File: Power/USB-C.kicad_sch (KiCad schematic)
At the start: 27 parts, among them J1 USB_C_Receptacle_PowerOnly_6P, J2 Barrel_Jack_Switch, J3 Barrel_Jack_Switch, J4 Barrel_Jack_Switch, J5 Barrel_Jack_Switch, U1 HUSB237, U2 TPS73801

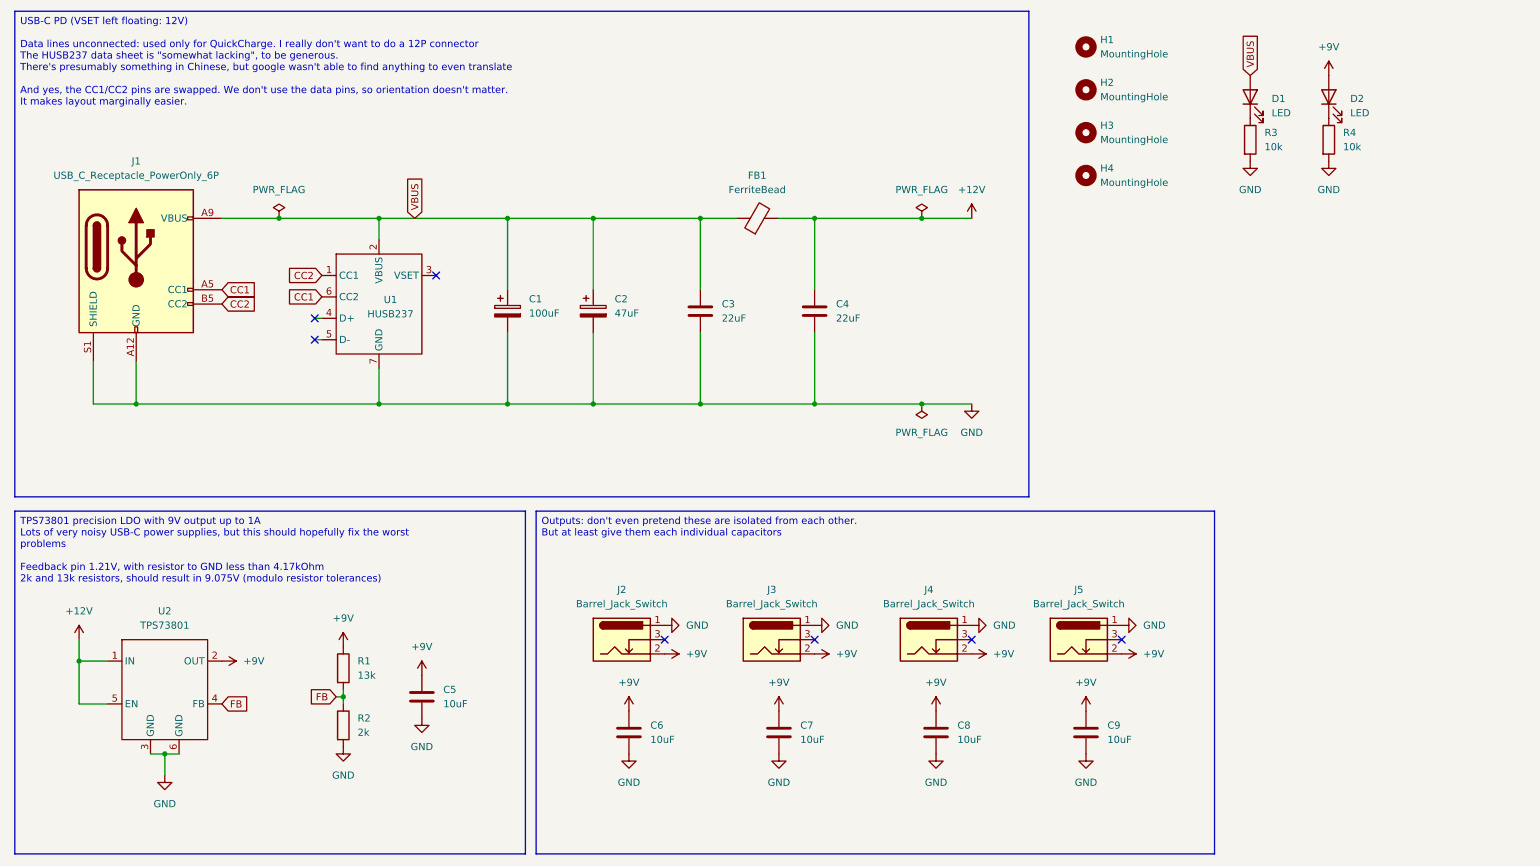
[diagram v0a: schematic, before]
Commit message: Make a switchable combo version of the USB-PD power board
So this was triggered partly by me noticing that my USB PD sources are
very inconsistent when it comes to 12V output that the original board
requested.

Several of my wall chargers do 15V but not 12V.  Of course, then some of
my battery packs are the reverse, and do 12V but not 15V output.

So there is no single thing that works for all common cases.  But 15V is
the more common option, and is required by the PD specs for anything
that claims to be 45W or more.  12V is entirely optional.

End result: add a switch to pick whether the power board requests 12V or
15V from the USB-C PD source.

And since 15V is now an option, add another LDO, and a switch to make
that LDO generate either 9V or 12V output (as per commit eb97091: "Add a
USB-C pedal power board" that already mentioned this option).

Connect the LDOs to two ports each, which also results in a certain
amount of isolation.

End result: the first two ports always output 9V, while the second two
ports can optionally provide 12V output if your USB-PD source does 15V.

The "switch" is either just a pin header with a jumper, or one of the
small slide switches that I have.  We're not doing anything fancy here.

Signed-off-by: Linus Torvalds <torvalds@linux-foundation.org>
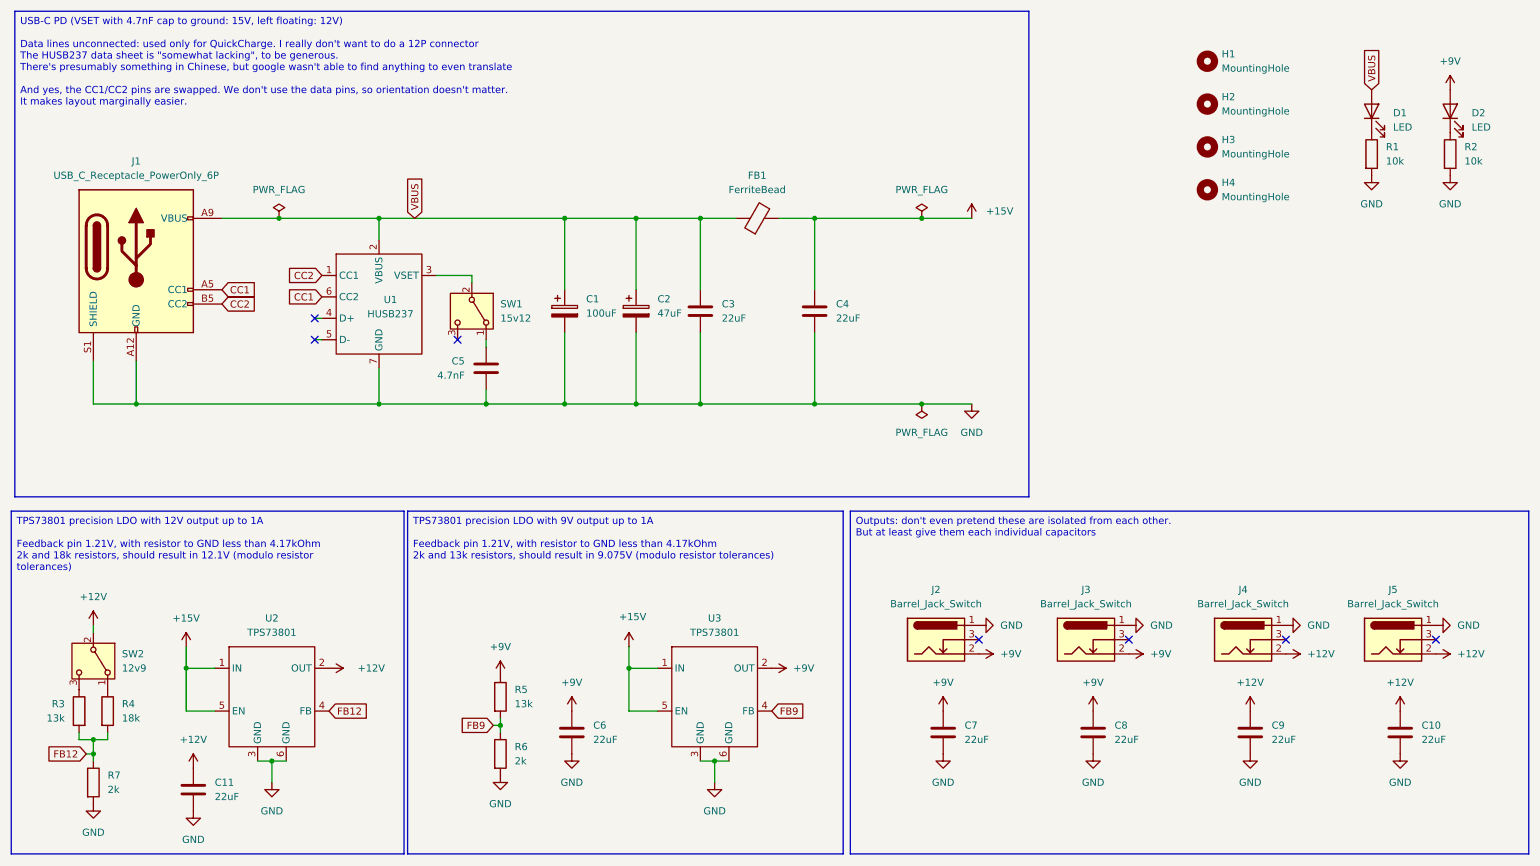
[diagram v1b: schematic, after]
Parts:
- added C11: 22uF, Capacitor_SMD:C_1206_3216Metric_Pad1.33x1.80mm_HandSolder, symbol Device:C
- added C5: 4.7nF, Capacitor_SMD:C_0805_2012Metric_Pad1.18x1.45mm_HandSolder, symbol Device:C
- added R3: 13k, Resistor_SMD:R_0805_2012Metric_Pad1.20x1.40mm_HandSolder, symbol Device:R
- added R4: 18k, Resistor_SMD:R_0805_2012Metric_Pad1.20x1.40mm_HandSolder, symbol Device:R
- added R7: 2k, Resistor_SMD:R_0805_2012Metric_Pad1.20x1.40mm_HandSolder, symbol Device:R
- added SW1: 15v12, Connector_PinSocket_2.54mm:PinSocket_1x03_P2.54mm_Vertical, symbol Switch:SW_SPDT
- added SW2: 12v9, Connector_PinSocket_2.54mm:PinSocket_1x03_P2.54mm_Vertical, symbol Switch:SW_SPDT
- added U2: TPS73801, Package_TO_SOT_SMD:SOT-223-6, symbol Mylib:TPS73801
- C10: renamed from C9; value 10uF -> 22uF
- C6: renamed from C5; value 10uF -> 22uF
- C7: renamed from C6; value 10uF -> 22uF
- C8: renamed from C7; value 10uF -> 22uF
- C9: renamed from C8; value 10uF -> 22uF
- renumbered R3 to R1, R4 to R2, R1 to R5, R2 to R6, U2 to U3
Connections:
- net +12V: now also C10.1, C9.1, J4.2, J5.2, C11.1, SW2.2 (B), U2.2 (OUT); no longer C4.1, FB1.2, U3.1 (IN), U3.5 (EN)
- net +9V: no longer C10.1, C9.1, J4.2, J5.2
- net GND: now also C11.2, C5.2, R7.2, U2.3 (GND), U2.6 (GND)
- net at U1.3 (VSET): now also SW1.2 (B)
- net FB renamed FB9
- new net: R4.1, SW2.1 (A)
- new net: R3.1, SW2.3 (C)
- new net: C5.1, SW1.1 (A)
- new net +15V: C4.1, FB1.2, U2.1 (IN), U2.5 (EN), U3.1 (IN), U3.5 (EN)
- new net FB12: R3.2, R4.2, R7.1, U2.4 (FB)
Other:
- moved on the sheet: C1, C10, C2, C6, C7, C8, C9, D1, D2, H1, H2, H3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

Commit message: Update USB-C pedal power board a bit more
Testing the old 12V-only board shows that several of my PD power
supplies that claim to only do 5V, 9V and 15V actually do 12V even if
they don't say so on the power supply.

It looks like 12V is common mainly due to Qualcomm Quick Charge (where
it is part of the spec), and so if the PD power supply does that, it
likely does 12V USB-PD too.

But having the switchable option is good regardless, and this adds a
updates the capacitor choices a bit.

I don't really have a great way to test power quality, but waving the
output end of the guitar pedal power supply next to a guitar cable that
is connected to the amp at the other end seems to be a good first
sanity-check.

And according to that simple check, the first (12V-only) pedal board is
fine.  Better than a commercial one I have around, in fact.  So these
may be quite usable.

Signed-off-by: Linus Torvalds <torvalds@linux-foundation.org>
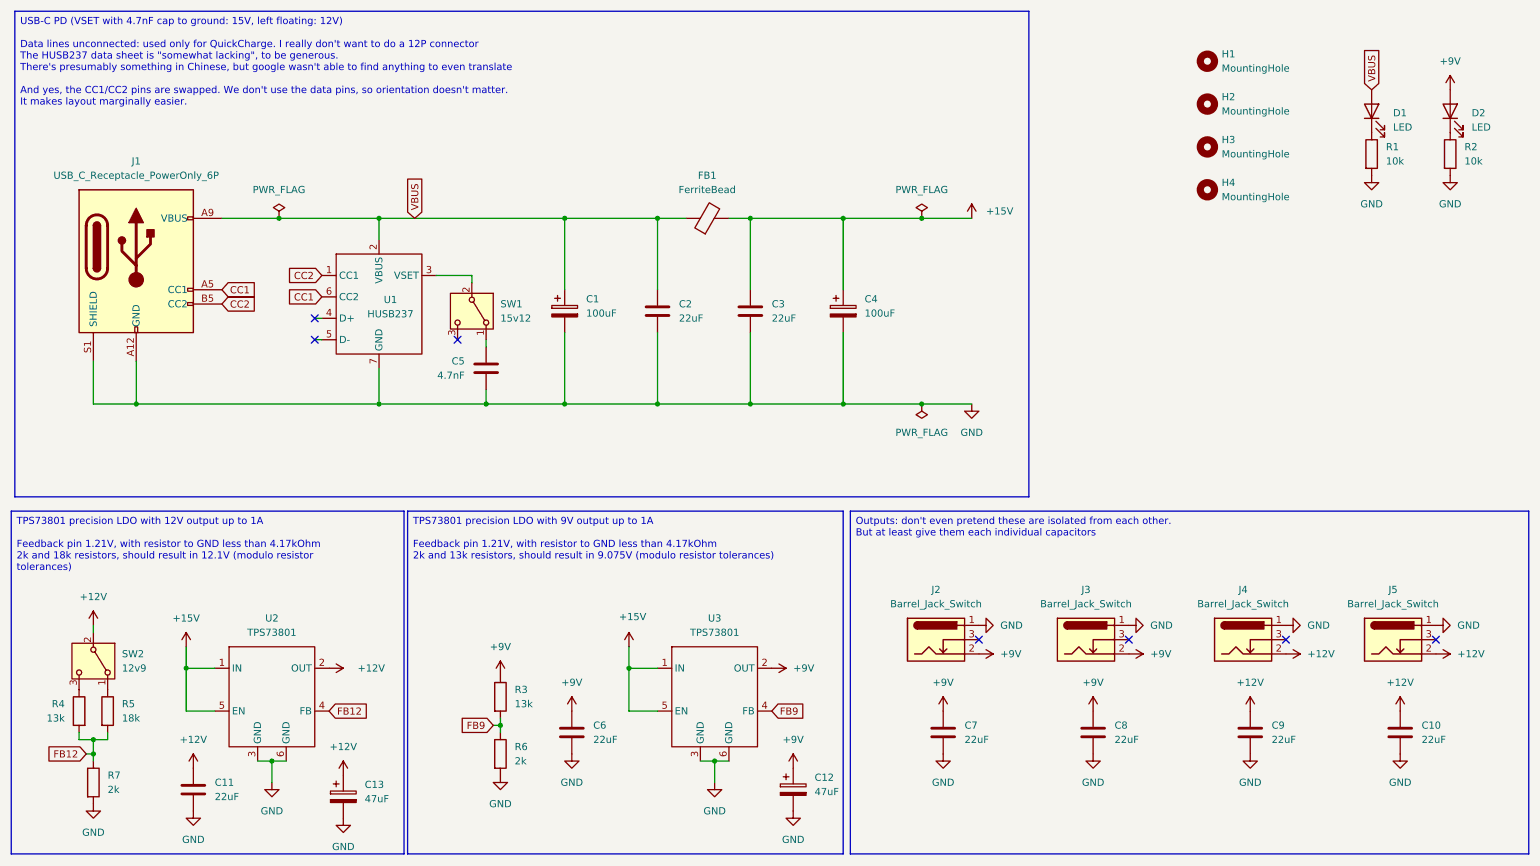
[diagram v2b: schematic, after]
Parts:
- added C12, C13: 47uF, Capacitor_THT:CP_Radial_D5.0mm_P2.00mm, symbol Device:C_Polarized
- C4: renamed from C2; value 47uF -> 100uF; footprint Capacitor_THT:CP_Radial_D5.0mm_P2.00mm -> Capacitor_THT:CP_Radial_D8.0mm_P3.50mm
- renumbered C3 to C2, C4 to C3, R5 to R3, R3 to R4, R4 to R5
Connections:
- net +12V: now also C13.1
- net +15V: now also C4.1
- net +9V: now also C12.1
- net GND: now also C12.2, C13.2
- net VBUS: no longer C4.1
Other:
- moved on the sheet: C2, C3, C4, FB1

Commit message: Do the ferrite bead on incoming power ground on the power board too
So I was looking at noise on my 5V test-board, and comparing the USB-C
power board to the Donner "real" guitar pedal power supply I have.  And
while my USB-C power board looks a bit better than the Donner on my
scope, I do see what very much looks like switching noise.

And I was comparing the VGND base board with the 5V one, and the bypass
signal on the VGND board really does look noticeably much better.  So
while that ferrite bead on the incoming ground started out as a "let's
try this", I'm becoming fairly convinced that it's meaningful.

Now, it probably isn't something that affects sound, because obviously
the bead just affects high-frequency noise.  We're definitely not
talking audio frequencies here.  But when it's visible on the scope, it
affects my ability to make judgment calls about other issues, so it
matters to me.

And who knows - noisy power might have an indirect effect on the opamps
or other chips, so cleaning it up can't be bad in general.

End result: let's just do the ferrite bead on the power supply board the
same way I did it on the 5V base board.  Separating those ground lines
just looks like the right thing to do and makes the board layout look
better anyway.

I don't know enough to actually believe in separate digital and analog
grounds, and I just do ground pours everywhere I can.  But filtering
incoming power lines is the kind of basic hygiene I can strive for.

Signed-off-by: Linus Torvalds <torvalds@linux-foundation.org>
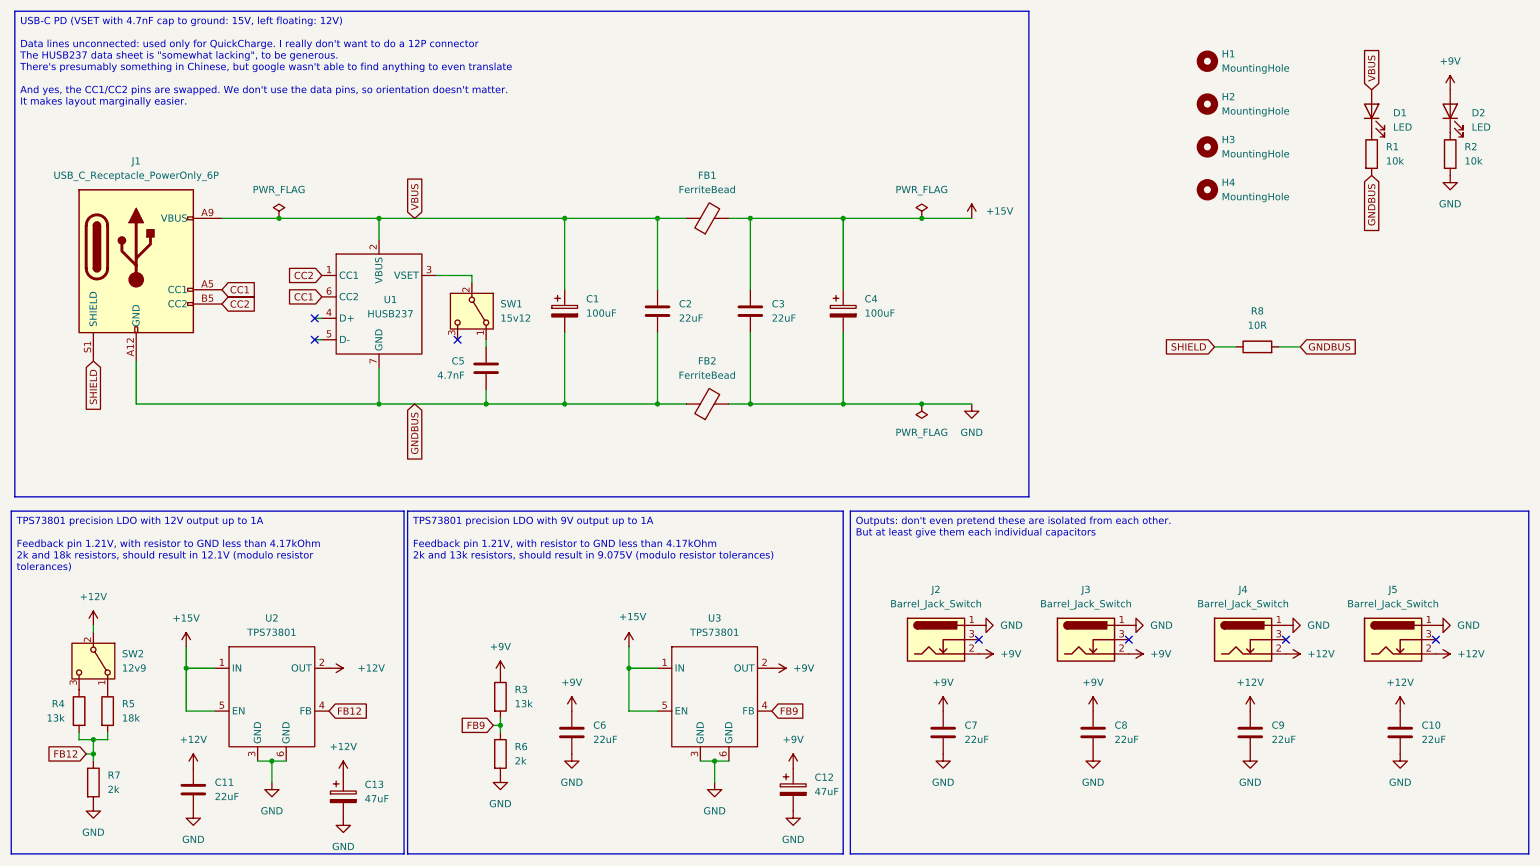
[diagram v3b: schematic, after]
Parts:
- added FB2: FerriteBead, Inductor_SMD:L_1206_3216Metric_Pad1.22x1.90mm_HandSolder, symbol Device:FerriteBead
- added R8: 10R, Resistor_SMD:R_0805_2012Metric_Pad1.20x1.40mm_HandSolder, symbol Device:R
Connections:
- net GND: now also FB2.2; no longer C1.2, C2.2, C5.2, J1.A12 (GND), J1.B12 (GND), J1.S1 (SHIELD), R1.2, U1.7 (GND)
- new net GNDBUS: C1.2, C2.2, C5.2, FB2.1, J1.A12 (GND), J1.B12 (GND), R1.2, R8.2, U1.7 (GND)
- new net SHIELD: J1.S1 (SHIELD), R8.1

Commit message: USB-C power board: do the common mode choke thing
It should probably go before the initial capacitor, but that would make
me have to lay out the board anew for this part, so I'm just doing a
minimal trial.  Any high-frequency common mode noise will bypass the cap
anyway, methinks.

Will this make any difference? Probably not, but let's see.

Signed-off-by: Linus Torvalds <torvalds@linux-foundation.org>
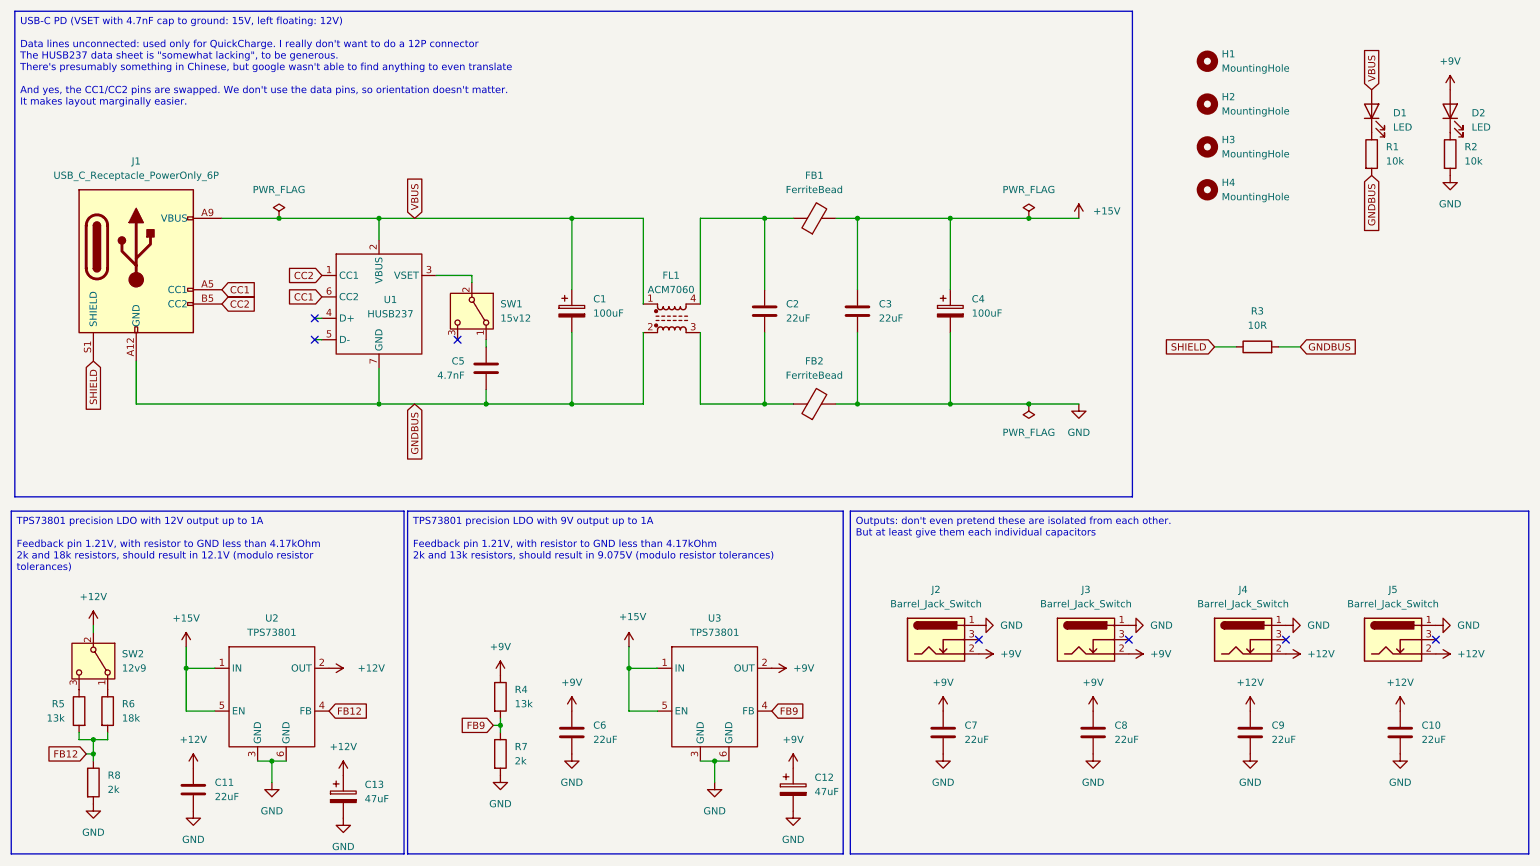
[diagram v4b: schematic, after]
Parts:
- added FL1: ACM7060, Inductor_SMD:L_CommonModeChoke_TDK_ACM7060, symbol Filter:Choke_CommonMode_FerriteCore_1423
- renumbered R8 to R3, R3 to R4, R4 to R5, R5 to R6, R6 to R7, R7 to R8
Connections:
- net GNDBUS: now also FL1.2; no longer C2.2, FB2.1
- net VBUS: now also FL1.1; no longer C2.1, FB1.1
- new net: C2.1, FB1.1, FL1.4
- new net: C2.2, FB2.1, FL1.3
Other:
- moved on the sheet: C1, C2, C3, C4, FB1, FB2

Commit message: USB-C power board: use the Würth reverse-mounted LEDs
This is the other board that had status lights on the non-SMD side.
Replace the through-hole LED with the reverse-mounted SMD ones.

Signed-off-by: Linus Torvalds <torvalds@linux-foundation.org>
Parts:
- D1, D2: footprint LED_THT:LED_D5.0mm -> Mylib:Würth Reverse Mount LED
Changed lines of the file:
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@@
 			)
 		)
-		(property "Footprint" "LED_THT:LED_D5.0mm"
+		(property "Footprint" "Mylib:Würth Reverse Mount LED"
 			(at 255.27 31.75 0)
 			(effects
@@
 			)
 		)
-		(property "Footprint" "LED_THT:LED_D5.0mm"
+		(property "Footprint" "Mylib:Würth Reverse Mount LED"
 			(at 269.24 31.75 0)
 			(effects
